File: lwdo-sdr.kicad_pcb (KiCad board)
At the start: 2 copper layers, 162 x 120 mm, 366 parts, among them J101 IN1, J102 IN2, J103 IN3, J104 IN4, J105 USB_B, J106 CLK_OUT, J107 REF_IN, J1401 Conn_02x10_Odd_Even, Q1201 NX7002AK, Q1202 PMN48XP, U1001 74LVC1G157, U1002 74LVC2G04, U1101 74LVC2GU04, U1102 74LVC2G04, U1201 TL431AFDT, U1202 TL431AFDT, U1203 TL431AFDT, U1204 MCP1824T-330, U1205 NCV8164ASN120T1G, U1206 MCP1824T-330, U1207 NCV8164ASN250T1G, U1208 NCV8164ASN330T1G, U1301 AT93C56, U1302 FT2232HL, U1401 74AVC4T245PW, U1402 74AVC4T245PW, U201 ICE40HX4K, U202 W25Q16JV, U203 IS61WV25616FBLL-10TLI, U301 THS4521ID, U401 THS4521ID, U501 THS4521ID, U601 THS4521ID, U701 AD7357xRU, U801 AD7357xRU, U901 DAC8551, U902 MCP1501-33xSN, U903 NCS325, U904 74LVC2GU04, U905 74LVC2G04, X901 DOT050V-020.0M, Y1301 12MHz CL=18p

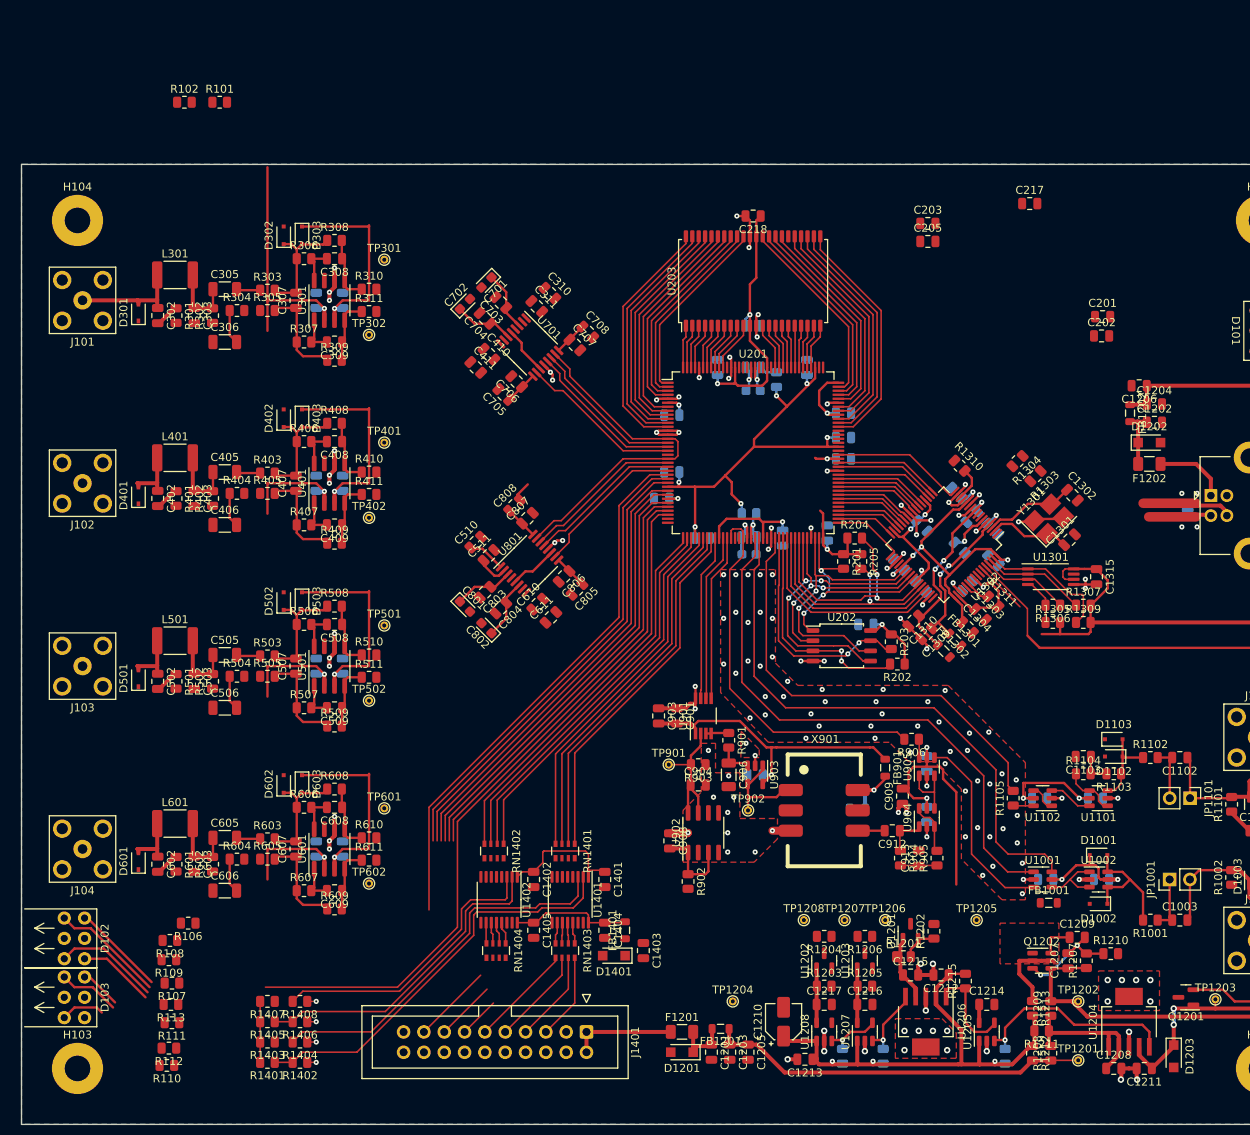
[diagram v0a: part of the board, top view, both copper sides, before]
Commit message: PCB: WIP Schematic: minor changes (decoupling, logic element ordering)
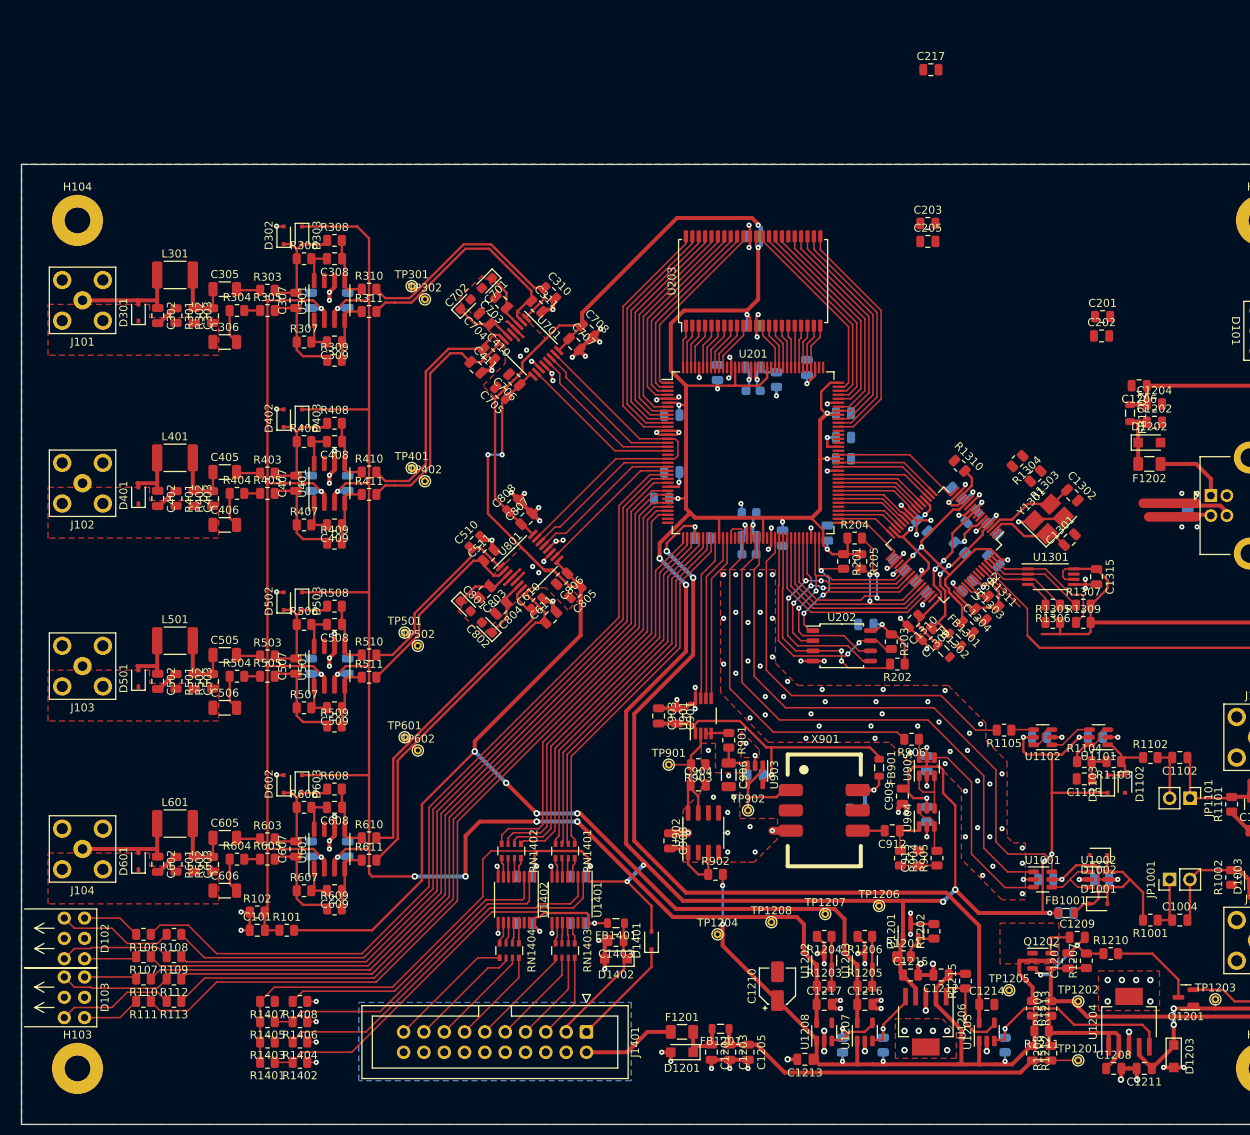
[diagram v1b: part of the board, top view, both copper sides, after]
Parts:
- added C1001: 100n, Capacitor_SMD:C_0805_2012Metric, B.Cu at (210.6, 123.6)
- added C101: 1u, Capacitor_SMD:C_0805_2012Metric, F.Cu at (109.5, 125.7)
- added D1401: BAT54J, Diode_SMD:D_SOD-323F, F.Cu at (158.8, 127.0)
- C1401, C1402, C1404, C1405, C218: moved to B.Cu
- C304, C404, C504, C604: value 100n -> 1u
- moved R101 103.8 mm to (113.2, 125.7)
- moved R102 101.6 mm to (109.5, 123.4)
- moved C217 20.8 mm to (193.7, 18.2)
- moved TP602 17.7 mm to (129.5, 103.3)
- moved R110 11.2 mm to (95.2, 131.8)
- moved C1404 10.1 mm to (142.9, 124.8), turned to 180 degrees
- moved TP1205 9.66 mm to (203.5, 133.2)
- moved TP601 9.25 mm to (127.9, 101.6)
- moved TP502 9.18 mm to (129.5, 90.2)
- moved R112 8.66 mm to (99.1, 131.8)
- moved TP1204 8.60 mm to (167.0, 126.2)
- moved R1105 8.59 mm to (202.8, 100.7), turned to 180 degrees
- moved TP402 8.35 mm to (130.4, 69.6)
- moved TP302 8.28 mm to (130.4, 46.9)
- moved C1104 7.62 mm to (214.2, 101.6)
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- renumbered C1001 to C1002, C1002 to C1003, C1003 to C1004, D1401 to D1402
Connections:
- net /ADC1/ADC.SCK renamed /ADC2/ADC.SCK
- net /Extension Connector/VDDEXT renamed /Extension Connector/VDDIO_CLEAN
- net /Extension Connector/VDDEXT_CABLE renamed /Extension Connector/VDDIO
- J1401 pad 1: /Extension Connector/OUT_5VEXT -> Net-(D1401-Pad1)
- R1105 pad 1: Net-(R1105-Pad1) -> Net-(U1102-Pad4)
- U1101 pad 1: Net-(R1104-Pad1) -> Net-(D1102-Pad1)
- U1101 pad 3: Net-(D1102-Pad1) -> Net-(R1104-Pad1)
- U1101 pad 4: Net-(R1104-Pad1) -> Net-(U1101-Pad4)
- U1101 pad 6: Net-(U1101-Pad6) -> Net-(R1104-Pad1)
- U1102 pad 1: Net-(U1102-Pad1) -> Net-(U1101-Pad4)
- U1102 pad 3: Net-(U1101-Pad6) -> Net-(U1102-Pad6)
- U1102 pad 4: Net-(U1102-Pad1) -> Net-(U1102-Pad4)
- U1102 pad 6: Net-(R1105-Pad1) -> Net-(U1102-Pad6)
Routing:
- net +3.3VD: track 173.1 -> 491.7 mm, vias 13 -> 26
- net +2.5VA: track 15.3 -> 173.0 mm, vias 0 -> 6
- net +3.3VA: track 144.9 -> 259.4 mm, vias 5 -> 9
- net AGND: track 154.6 -> 226.8 mm, vias 159 -> 205
- net +1.2VD: track 60.7 -> 121.4 mm, vias 6 -> 8
- net /Input Amplifier 1/VOCM: track 72.0 -> 121.1 mm
- net /FPGA/LED.IN_R3: track 55.8 -> 103.7 mm
- net /FPGA/LED.IN_G1: track 56.6 -> 103.7 mm
- net /FPGA/LED.IN_G4: track 53.8 -> 100.4 mm
- net /ADC2/INB+: track 0.00 -> 45.2 mm
- net /FPGA/LED.IN_R4: track 54.7 -> 99.5 mm
- net /ADC2/INB-: track 0.00 -> 42.5 mm
- net /FPGA/LED.IN_R2: track 58.6 -> 100.8 mm
- net /FPGA/LED.IN_G2: track 57.7 -> 99.9 mm
- net /FPGA/LED.IN_R1: track 68.1 -> 105.4 mm
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
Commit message: Update schematic: - Redesign of decoupling based on swcad modelling (predominantly use 1uf, no paralleled caps) - Reroute REF_CLK_IN, CLK_SEL net to different FPGA pins - Some net renaming - Ext conn: add decoupling to 3v3 output - Reassign references to all components PCB: routing almost finished
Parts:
- removed the C1201 at (166.2, 141.0)
- removed the C1205 at (170.8, 141.0)
- removed C1216, C1217: 1u, Capacitor_SMD:C_0805_2012Metric
- removed the C1405 at (149.6, 124.8)
- removed the C215 at (161.3, 61.3)
- removed the C216 at (185.5, 87.5)
- removed the C217 at (193.7, 18.2)
- removed the C218 at (171.4, 39.0)
- removed C219: 100n, Capacitor_SMD:C_0805_2012Metric
- removed the C905 at (184.5, 110.6)
- removed the C910 at (193.2, 111.3)
- removed the C911 at (193.2, 104.9)
- removed the R1303 at (206.8, 69.0)
- removed the R1304 at (204.5, 67.1)
- removed R1310: 10k, Resistor_SMD:R_0805_2012Metric
- added C1209: 1u, Capacitor_SMD:C_0805_2012Metric, F.Cu at (220.3, 143.0)
- added C1210: 4.7u, Capacitor_SMD:C_0805_2012Metric, B.Cu at (198.5, 140.1)
- added C1316: 1u, Capacitor_SMD:C_0805_2012Metric, F.Cu at (198.1, 87.8)
- added C1404: 1u, Capacitor_SMD:C_0805_2012Metric, F.Cu at (157.9, 124.8)
- added C1406: 1u, Capacitor_SMD:C_0805_2012Metric, B.Cu at (142.9, 124.8)
- added C908: 1u, Capacitor_SMD:C_0805_2012Metric, B.Cu at (193.2, 111.3)
- C1001, C1003, C1104, C1202, C1203, C1204, C1305, C1306, C1307, C1308, C1312, C1314, C1401, C1402, C1403, C204, C206, C207, C208, C209, C210, C211, C212, C213, C214: value 100n -> 1u
- C1206, C1309, C1310: value 4.7u -> 1u
- C1211, C1212, C1213, C1214, C1215, C301, C401, C501, C601: value 1u -> 4.7u
- C1301, C1302, C205, C903: moved to B.Cu
- C1303, C1304, C201, C202, C203, C909: value 4.7u -> 1u; moved to B.Cu
- C1311, C1313: value 100n -> 1u; moved to F.Cu
- C1315, C901: value 100n -> 1u; moved to B.Cu
- C705: renamed from C706; value 100n -> DNP
- C708: renamed from C707; value 100n -> DNP
- C805: renamed from C806; value 100n -> DNP
- C808: renamed from C807; value 100n -> DNP
- C902: value 100n -> 4.7u; moved to F.Cu
- moved TP102 180.4 mm to (205.7, 111.8), turned to 90 degrees
- moved H105 163.2 mm to (165.0, 131.0)
- moved R104 93.5 mm to (224.8, 50.8)
- moved R103 90.9 mm to (224.8, 53.0)
- moved R105 90.7 mm to (224.8, 48.6)
- moved C1206 85.4 mm to (216.5, 143.0), turned to 0 degrees
- moved R1302 80.4 mm to (222.2, 88.4), turned to -90 degrees
- moved R1301 77.9 mm to (224.4, 88.4), turned to -90 degrees
- moved TP101 74.2 mm to (101.6, 81.3), turned to 180 degrees
- moved C205 46.6 mm to (165.1, 76.7)
- moved C202 43.6 mm to (171.4, 50.2)
- moved C1201 43.2 mm to (173.4, 142.4), turned to -90 degrees
- moved C201 34.6 mm to (182.8, 61.1)
- moved C213 33.0 mm to (185.5, 87.5), turned to 180 degrees
- moved FB1202 32.3 mm to (230.0, 91.3), turned to 0 degrees
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- renumbered C1208 to C1201, C1207 to C1205, C1209 to C1207, C1210 to C1208, C1404 to C1405, C220 to C215, C221 to C216, C222 to C217, C223 to C218, C705 to C706, C708 to C707, C805 to C806, C808 to C807, C907 to C905, C908 to C907, C912 to C910, C913 to C911, D1402 to D1401, D1401 to D1402, R1305 to R1303, R1306 to R1304, R1307 to R1305, R1308 to R1306, R1309 to R1307, R1311 to R1308
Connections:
- net /Extension Connector/OUT_5VEXT renamed /Extension Connector/5VEXT
- net Net-(D1401-Pad1) renamed /Extension Connector/EXT_VDD3V3
- C1201 pad 1: /Power Supply/+5VFTDI -> Net-(C1201-Pad1)
- C1206 pad 1: /Power Supply/VBUS_CLEAN -> /Power Supply/+5VFTDI
- C1211 pad 1: /FTDI/FT_3V3 -> +5VMAIN
- C1212 pad 1: +5VMAIN -> +1.2VD
- C1213 pad 1: +5VMAIN -> +3.3VD
- C1214 pad 1: +1.2VD -> +2.5VA
- C1215 pad 1: +3.3VD -> +3.3VA
- C1304 pad 1: /FTDI/FT_+1V8 -> /FTDI/FT_3V3
- C1309 pad 1: /FTDI/FT_VPHY -> /FTDI/FT_3V3
- C1310 pad 1: /FTDI/FT_VPLL -> /FTDI/FT_VPHY
- C1311 pad 1: /FTDI/FT_3V3 -> /FTDI/FT_VPLL
- C1313 pad 1: /FTDI/FT_VPHY -> /FTDI/FT_3V3
- C1314 pad 1: /FTDI/FT_VPLL -> /FTDI/FT_VPHY
- C1315 pad 1: /FTDI/FT_3V3 -> /FTDI/FT_VPLL
- C1403 pad 1: /Extension Connector/VDDIO -> /Extension Connector/EXT_VDDIO
- C1405 pad 1: /Extension Connector/VDDIO_CLEAN -> /Extension Connector/VDDIO
- C211 pad 1: +1.2VD -> +3.3VD
- C213 pad 1: +1.2VD -> +3.3VD
- D1001 pad 1: /Clock Output/VDD_3V3 -> +3.3VD
- D1401 pad 1: /Extension Connector/VDDIO -> /Extension Connector/EXT_VDDIO
- FB1401 pad 1: /Extension Connector/VDDIO -> /Extension Connector/EXT_VDDIO
- FB1401 pad 2: /Extension Connector/VDDIO_CLEAN -> /Extension Connector/VDDIO
- J1401 pad 3: /Extension Connector/VDDIO -> /Extension Connector/EXT_VDDIO
- U1302 pad 14: Net-(R1310-Pad2) -> /FTDI/FT_3V3
- U1302 pad 7: /FTDI/USB_DR- -> /FTDI/USB_D-
- U1302 pad 8: /FTDI/USB_DR+ -> /FTDI/USB_D+
- U1401 pad 16: /Extension Connector/VDDIO_CLEAN -> /Extension Connector/VDDIO
- U1402 pad 16: /Extension Connector/VDDIO_CLEAN -> /Extension Connector/VDDIO
- U201 pad 56: /Clock Output/CLK_SEL -> /FPGA/REF_CLK_IN
- U201 pad 60: /FPGA/REF_CLK_IN -> /Clock Output/CLK_SEL
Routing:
- net +3.3VD: track 491.7 -> 595.8 mm, vias 26 -> 24
- net /FPGA/LED.STS_R: track 0.00 -> 48.0 mm
- net +1.2VD: track 121.4 -> 168.8 mm, vias 8 -> 11
- net /FPGA/LED.STS_G: track 0.00 -> 47.4 mm
- net /Power Supply/VBUS_CLEAN: track 143.4 -> 102.0 mm
- net /FTDI/~{PWRSAV}: track 6.54 -> 41.6 mm, vias 0 -> 4
- net /FTDI/FT_3V3: track 154.5 -> 181.6 mm, vias 6 -> 8
- net /FTDI/USB_D-: track 9.19 -> 32.9 mm, vias 0 -> 1
- net /FTDI/USB_D+: track 12.7 -> 36.3 mm, vias 0 -> 1
- net +3.3VA: track 259.4 -> 282.5 mm, vias 9 -> 12
- net AGND: track 226.8 -> 245.7 mm, vias 205 -> 218
- net /Extension Connector/EXT_VDDIO: track 0.00 -> 16.9 mm
- net /Power Supply/VBUS: track 9.16 -> 25.2 mm
- net /Extension Connector/VDDIO_CLEAN: track 14.9 -> 0.00 mm, vias 2 -> 0
- net Net-(D101-Pad6): track 0.00 -> 12.6 mm
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
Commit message: PCB: enable fillets for some zones, fix DRC errors
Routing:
- net AGND: track 245.7 -> 252.6 mm, vias 218 -> 220
- net /VCXO/VCXO_VCC: track 8.09 -> 5.58 mm
- net /Extension Connector/DIR78: track 36.9 -> 39.2 mm
- net /Extension Connector/DIR34: track 45.6 -> 47.9 mm
- net Net-(R1214-Pad1): track 26.6 -> 25.4 mm
- net Net-(D103-Pad1): track 7.32 -> 6.69 mm

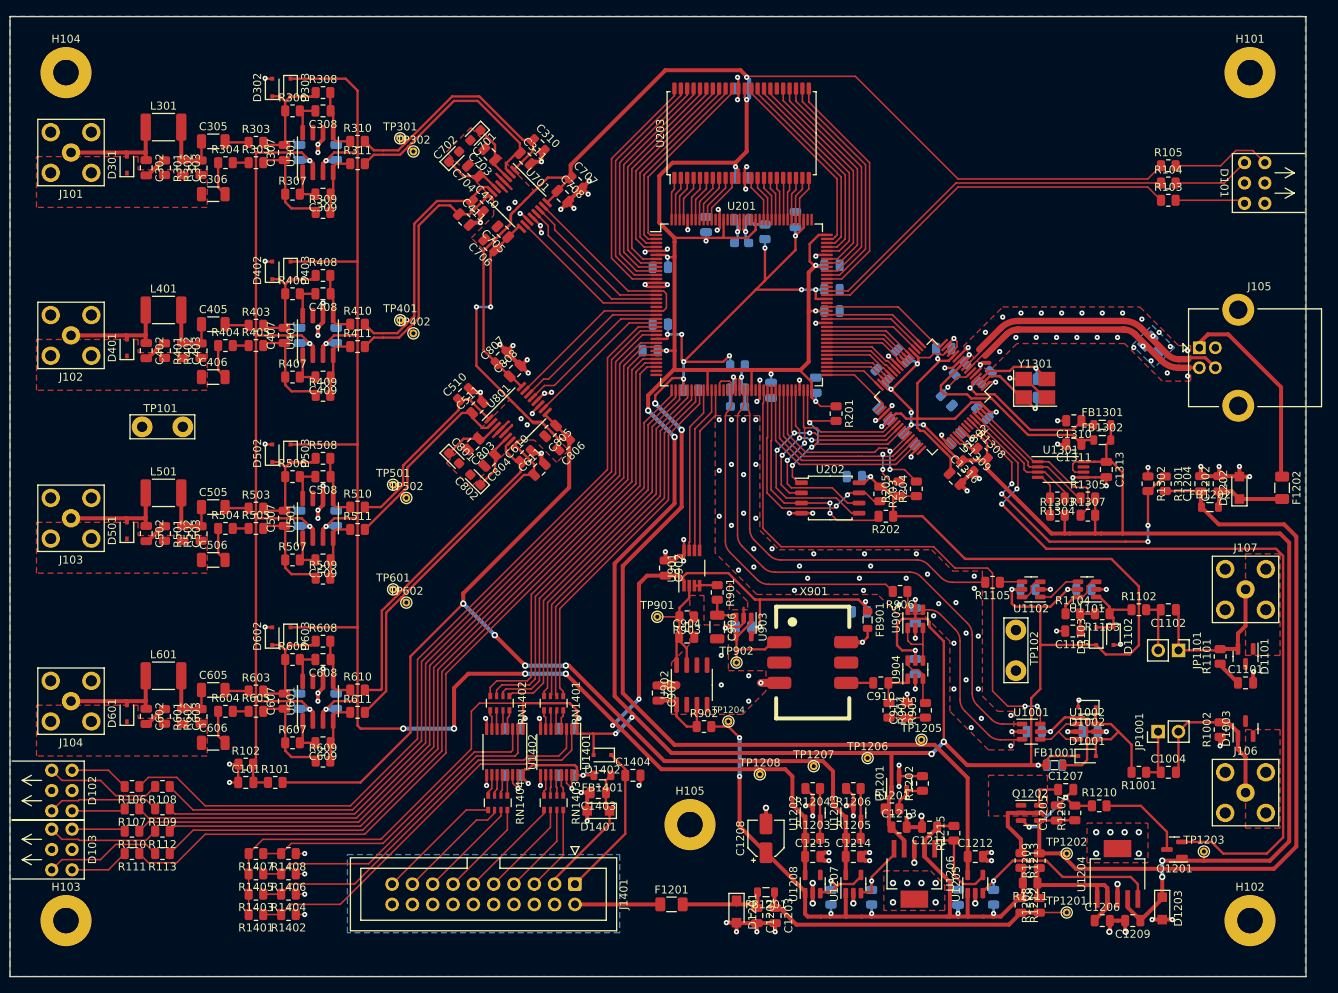
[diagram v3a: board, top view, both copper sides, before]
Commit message: PCB: top silkscreen done
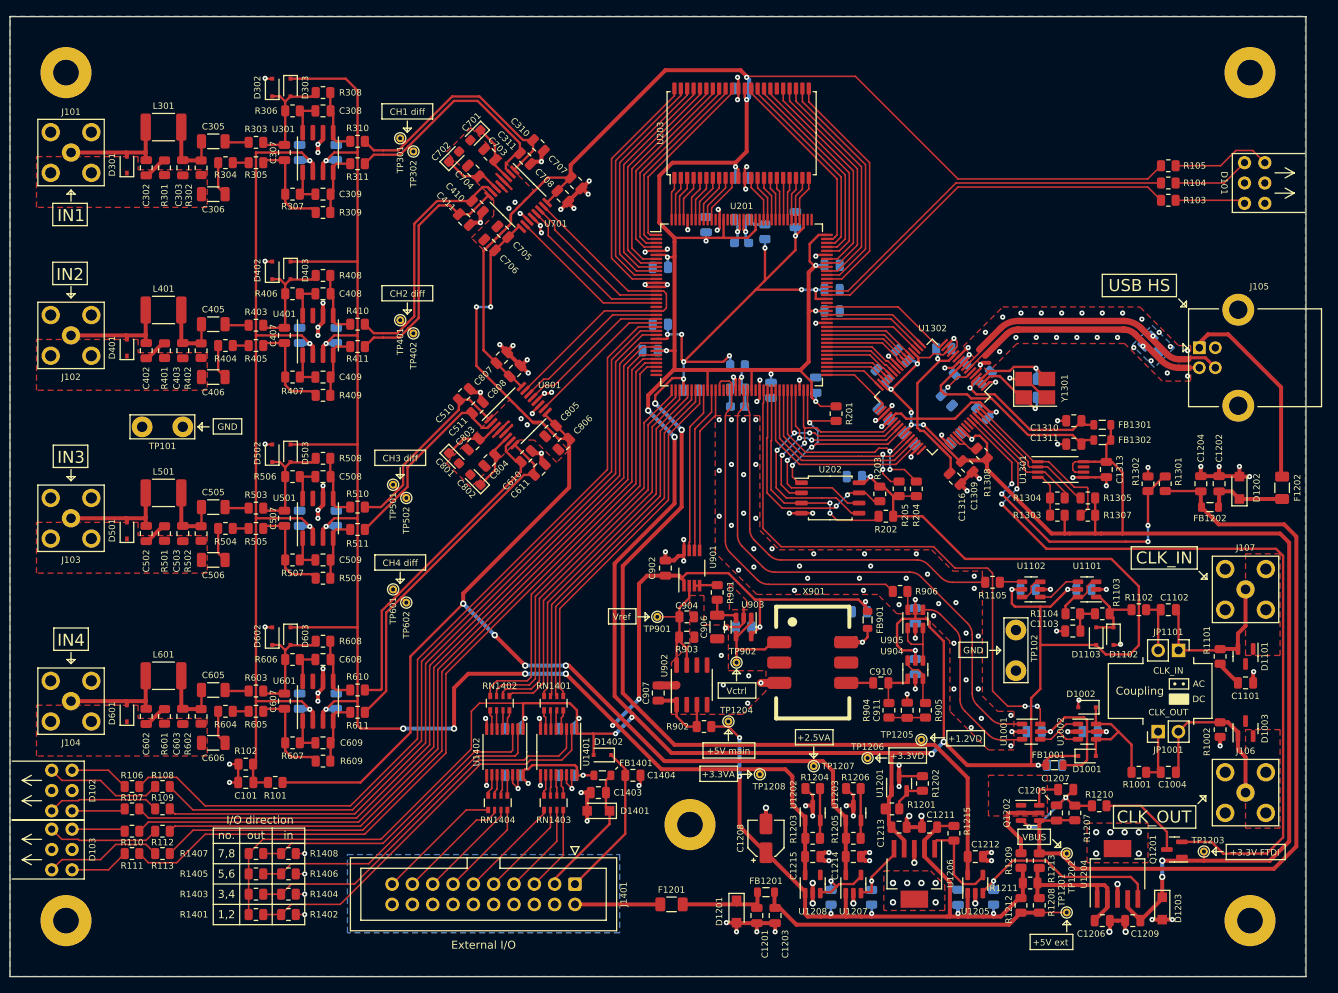
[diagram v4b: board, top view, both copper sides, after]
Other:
- board text added: "+1.2VD"
- board text added: "+2.5VA"
- board text added: "+3.3V FTDI"
- board text added: "+3.3VA"
- board text added: "+3.3VD"
- board text added: "+5V ext"
- board text added: "+5V main"
- board text added: "1,2"
- board text added: "3,4"
- board text added: "5,6"
- board text added: "7,8"
- board text added: "AC"
- board text added: "CH1 diff"
- board text added: "CH2 diff"
- board text added: "CH3 diff"
- board text added: "CH4 diff"
- board text added: "CLK_IN"
- board text added: "CLK_OUT"
- board text added: "Coupling"
- board text added: "DC"
- board text added: "External I/O"
- board text added: "GND"
- board text added: "I/O direction"
- board text added: "IN1"
- board text added: "IN2"
- board text added: "IN3"
- board text added: "IN4"
- board text added: "USB HS"
- board text added: "VBUS"
- board text added: "Vctrl"
- board text added: "Vref"
- board text added: "in"
- board text added: "no."
- board text added: "out"
